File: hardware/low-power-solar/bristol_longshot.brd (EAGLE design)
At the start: 40 x 82 mm, 143 parts, among them Q1 NX2301P, Q2 NX2301P, Q3 BSS84, Q4 BSS84, Q5 PBSS4130, Q6 PD84001, U1 SAM_D20E, U10 TPS71533DCKR, U11 TPS73118DBVT, U12 LTC4070EMS8EPBF, U13 74LVC1G04GW, U14 SIT1552, U15 74LVC1G04GW, U16 SIT1552, U17 TPS71533DCKR, U18 74LVC1G04GW, U2 SI4461, U3 SE880, U4 SST25WF040BT-40I/NP, U5 TG-5006CJ, U6 ADP1614ACPZ-1.3-R7, U7 ADM6823WYRJZ, U8 SN74LVC1G32DCKR, U9 TPS62243

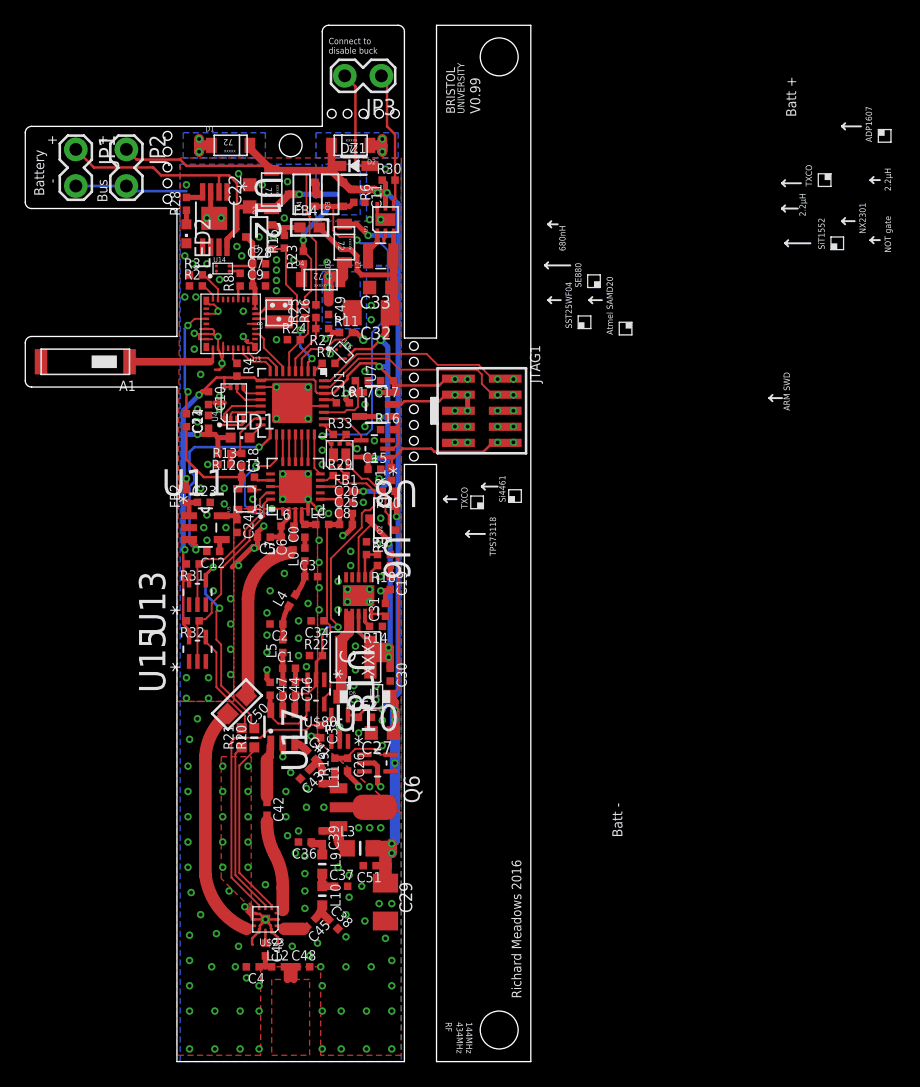
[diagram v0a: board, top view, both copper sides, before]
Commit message: [low-power-solar] complete IC section of partslist, board order
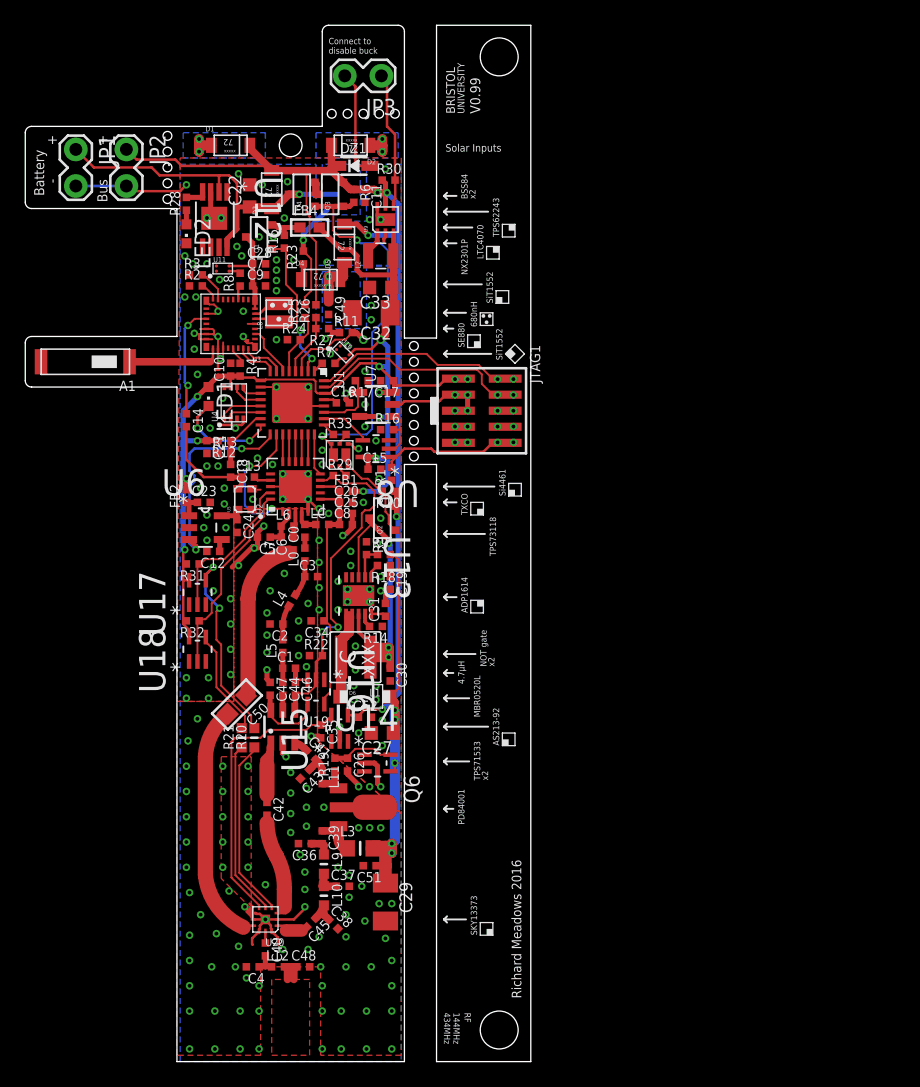
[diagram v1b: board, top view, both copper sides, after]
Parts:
- L1: value XFL4030-4.7µF -> XFL4030-4.7µH
- R29, R33: value 1kΩ -> 100kΩ
- R6: value 1MΩ -> 100kΩ
- U10: value TPS71533DCKR -> SIT1552; device TPS71533DCKR:SOT65P210X110-5N -> fbri:SIT1552
- U11: value TPS73118DBVT -> SIT1552; device TPS73118DVBT:SOT95P280X145-5N -> fbri:SIT1552
- U13: value 74LVC1G04GW -> ADP1614ACPZ-1.3-R7; device 74LVC1G04GW_inverter:SOT65P210X110-5N -> ADP1614:DFN50P300X300X80-11N
- U14: value SIT1552 -> TPS71533DCKR; device fbri:SIT1552 -> TPS71533DCKR:SOT65P210X110-5N
- U15: value 74LVC1G04GW -> TPS71533DCKR; device 74LVC1G04GW_inverter:SOT65P210X110-5N -> TPS71533DCKR:SOT65P210X110-5N
- U16: value SIT1552 -> 74LVC1G04GW; device fbri:SIT1552 -> 74LVC1G04GW_inverter:SOT65P210X110-5N
- U17: value TPS71533DCKR -> 74LVC1G04GW; device TPS71533DCKR:SOT65P210X110-5N -> 74LVC1G04GW_inverter:SOT65P210X110-5N
- U6: value ADP1614ACPZ-1.3-R7 -> TPS73118DBVT; device ADP1614:DFN50P300X300X80-11N -> TPS73118DVBT:SOT95P280X145-5N
- moved U14 41.0 mm to (27.9, 23.6)
- moved U10 32.6 mm to (25.1, 56.1), turned to 315 degrees
- moved U16 27.0 mm to (23.0, 29.2), turned to 270 degrees
- moved U11 20.5 mm to (15.6, 62.8)
- moved U17 15.6 mm to (13.6, 37.1)
- moved U6 13.3 mm to (14.2, 42.2), turned to 0 degrees
- moved U15 12.9 mm to (24.9, 26.4)
- moved U13 12.8 mm to (26.4, 36.9), turned to 270 degrees
- moved U18 9.96 mm to (13.6, 32.6), turned to 90 degrees
- moved LED1 4.10 mm to (14.5, 52.6), turned to 180 degrees
- moved C10 2.85 mm to (16.2, 54.8), turned to 90 degrees
- moved C21 2.00 mm to (14.4, 48.6), turned to 270 degrees
- moved C18 1.24 mm to (16.2, 46.8)
- moved R12 1.00 mm to (15.8, 49.1)
- moved R13 0.88 mm to (15.8, 48.1)
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- renumbered U$23 to U20, U$80 to U19
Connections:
- net 1.8V: now also U10.3, U17.5, U18.5; no longer U13.5, U15.5, U16.3
- net 7.5V: now also U14.4; no longer U10.4
- net BOOST_COMP: now also U13.1; no longer U6.1
- net BOOST_CURRENTLIMIT: now also U13.9; no longer U6.9
- net BOOST_FB: now also U13.2; no longer U6.2
- net BOOST_SOFTSTART: now also U13.10; no longer U6.10
- net BOOST_SUPPLY: now also U13.3, U13.8; no longer U6.3, U6.8
- net BOOST_SW: now also U13.6, U13.7; no longer U6.6, U6.7
- net GND: now also U10.1, U10.4, U11.1, U11.4, U13.11, U13.4, U13.5, U14.2, U15.2, U16.3, U17.3, U6.2; no longer U10.2, U11.2, U13.3, U14.1, U14.4, U15.3, U16.1, U16.4, U17.2, U6.11, U6.4, U6.5
- net GPS_VDD_SWITCHED: now also U11.3; no longer U14.3
- net LF_CLOCK_OUT: now also U10.2; no longer U16.2
- net RADIO_VDD: now also U16.5; no longer U18.5
- net RF_SW_V2: now also U16.4; no longer U18.4
- net RF_TCXO_REG_EN: now also U6.3; no longer U11.3
- net SE800_LF_OUT: now also U11.2; no longer U14.2
- net SI_GPIO0: now also U16.2; no longer U18.2
- net SI_GPIO2: now also U17.2; no longer U13.2
- net SI_GPIO3: now also U18.2; no longer U15.2
- net SKY_V1_1: now also U17.4; no longer U13.4
- net SKY_V2_1: now also U18.4; no longer U15.4
- net TCXO_REG_IN: now also U6.1; no longer U11.1
- net TCXO_REG_NR: now also U6.4; no longer U11.4
- net TCXO_VDD: now also U6.5; no longer U11.5
- net V_BUS: now also U15.4; no longer U17.4
- net V_GG: now also U14.5; no longer U10.5
- net V_SKY: now also U15.5; no longer U17.5
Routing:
- net LED1: track 1.36 -> 8.26 mm, vias 0 -> 2
- net 1.8V: track 99.6 -> 96.3 mm
- net GND: track 94.1 -> 96.2 mm, vias 215 -> 216
- net BYPASS: track 8.14 -> 9.24 mm
- net SAM_XOSC: track 5.58 -> 4.96 mm
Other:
- board text added: "4.7µH"
- board text added: "ADP1614"
- board text added: "AS213-92"
- board text added: "BSS84"
- board text added: "LTC4070"
- board text added: "MBR0520L"
- board text added: "NX2301P"
- board text added: "PD84001"
- board text added: "SKY13373"
- board text added: "Solar Inputs"
- board text added: "TPS62243"
- board text added: "TPS71533"
- board text added: "x2"
- board text removed: "18mm wide, lli-ion battery is ~19mm"
- board text removed: "2.2µH"
- board text removed: "ADP1607"
- board text removed: "ARM SWD"
- board text removed: "Atmel SAMD20"
- board text removed: "Batt +"
- board text removed: "Batt -"
- board text removed: "NX2301"
- board text removed: "SST25WF04"
- board text removed: "University of BRISTOL"
